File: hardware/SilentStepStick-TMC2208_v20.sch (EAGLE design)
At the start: 24 parts, among them IC1 TMC2208-LA, J1 MA08-1, J2 MA08-1, J3 MA02-1, X1 PASSER-04, X2 PASSER-04

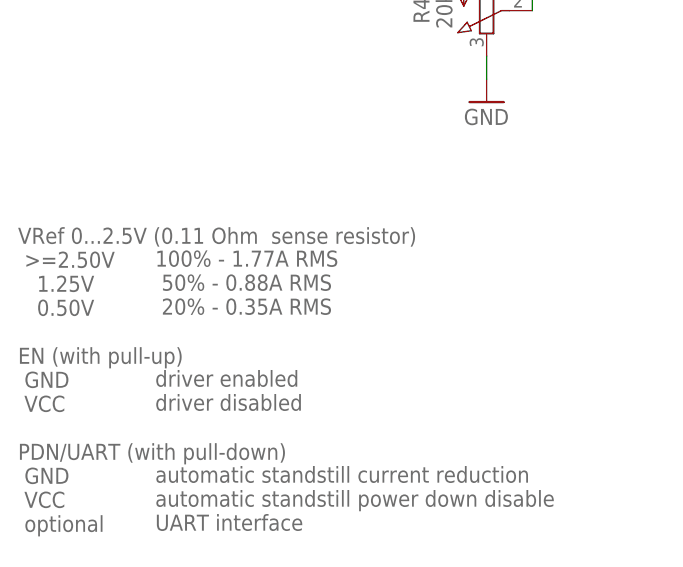
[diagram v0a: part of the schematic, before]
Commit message: corrected Vref and current values
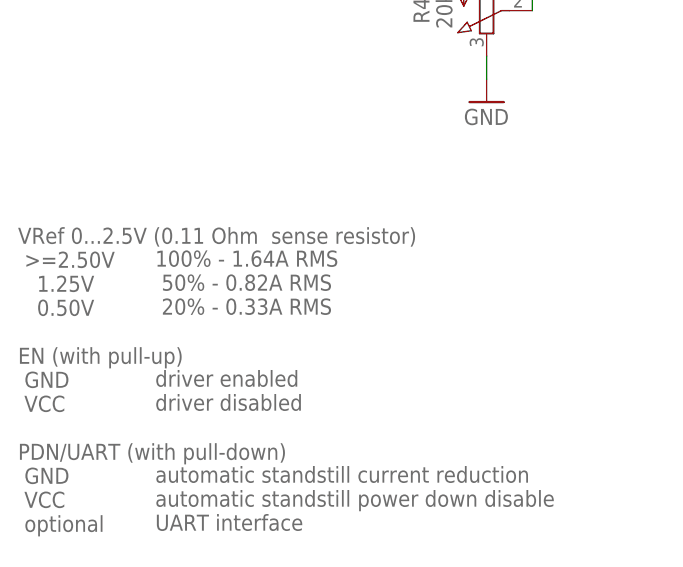
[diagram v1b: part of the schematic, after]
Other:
- note added: "100% - 1.64A RMS 50% - 0.82A RMS 20% - 0.33A RMS driver enabled driver disabled automatic standstill current reduction automatic standstill power down disable UART interface"
- note removed: "100% - 1.77A RMS 50% - 0.88A RMS 20% - 0.35A RMS driver enabled driver disabled automatic standstill current reduction automatic standstill power down disable UART interface"
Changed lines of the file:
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@@
  VCC
  optional</text>
-<text x="38.1" y="55.88" size="1.778" layer="95" font="vector" ratio="10" align="top-left">100% - 1.77A RMS
- 50% - 0.88A RMS
- 20% - 0.35A RMS
+<text x="38.1" y="55.88" size="1.778" layer="95" font="vector" ratio="10" align="top-left">100% - 1.64A RMS
+ 50% - 0.82A RMS
+ 20% - 0.33A RMS
 driver enabled
 driver disabled
